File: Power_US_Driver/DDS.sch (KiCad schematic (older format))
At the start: 3 parts, among them U3 AD9833_MOD

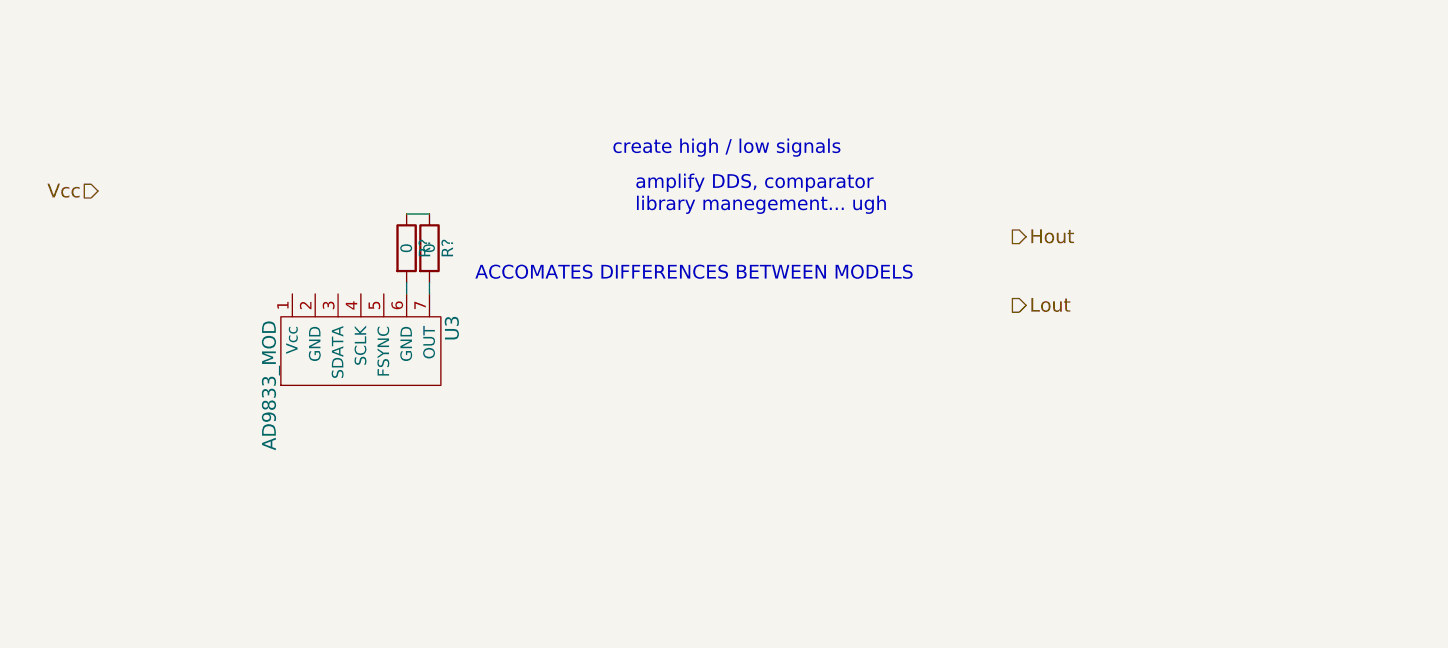
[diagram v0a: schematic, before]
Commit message: CURRENT SENSE REROUT, HIGHSIDE DRIVER GROUNDING
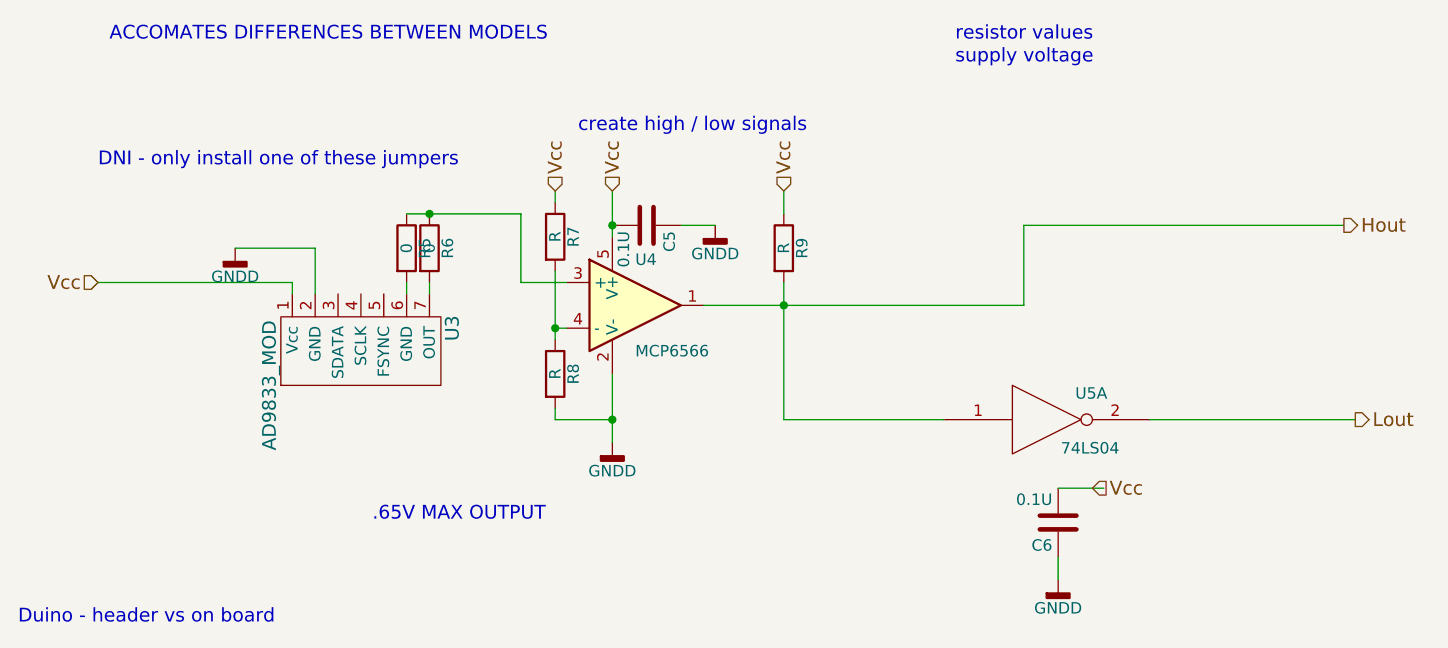
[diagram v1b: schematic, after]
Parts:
- added C5, C6: 0.1U, symbol C
- added R7, R8, R9: R, symbol R
- added U4: MCP6566, symbol MCP6566
- added U5: 74LS04, symbol 74LS04
- gave numbers to parts that had none: 2
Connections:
- net labels added: GNDD
- wire segments 3 -> 26
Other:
- note added: ".65V MAX OUTPUT"
- note added: "DNI - only install one of these jumpers"
- note added: "Duino - header vs on board"
- note added: "resistor values"
- note added: "supply voltage"
- note removed: "amplify DDS, comparator\nlibrary manegement... ugh"
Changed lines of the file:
@@
 LIBS:LIA-cache
 LIBS:power_US
+LIBS:JasMoH_Parts
 LIBS:Power_US_Driver-cache
 EELAYER 25 0
@@
 	0    -1   1    0
 $EndComp
-Text Notes 5450 3050 0    60   ~ 0
+Text Notes 5300 2950 0    60   ~ 0
 create high / low signals
-Text HLabel 3200 3200 0    60   Input ~ 0
-Vcc
-Text HLabel 7200 3400 2    60   Output ~ 0
+Text HLabel 3200 3600 0    60   Input ~ 0
+Vcc
+Text HLabel 8650 3350 2    60   Output ~ 0
 Hout
-Text HLabel 7200 3700 2    60   Output ~ 0
+Text HLabel 8700 4200 2    60   Output ~ 0
 Lout
-Text Notes 5550 3300 0    60   ~ 0
-amplify DDS, comparator\nlibrary manegement... ugh
-$Comp
-L R R?
+$Comp
+L R R5
 U 1 1 5AB00777
 P 4550 3450
-F 0 "R?" V 4630 3450 50  0000 C CNN
+F 0 "R5" V 4630 3450 50  0000 C CNN
 F 1 "0" V 4550 3450 50  0000 C CNN
 F 2 "" V 4480 3450 50  0001 C CNN
@@
 $EndComp
 $Comp
-L R R?
+L R R6
 U 1 1 5AB0079E
 P 4650 3450
-F 0 "R?" V 4730 3450 50  0000 C CNN
+F 0 "R6" V 4730 3450 50  0000 C CNN
 F 1 "0" V 4650 3450 50  0000 C CNN
 F 2 "" V 4580 3450 50  0001 C CNN
@@
 	1    0    0    -1
 $EndComp
-Wire Wire Line
-	4650 3300 4550 3300
+Text Notes 3250 2550 0    60   ~ 0
+ACCOMATES DIFFERENCES BETWEEN MODELS
+$Comp
+L GNDD #PWR5
+U 1 1 5AB1401C
+P 5450 4300
+F 0 "#PWR5" H 5450 4050 50  0001 C CNN
+F 1 "GNDD" H 5450 4175 50  0000 C CNN
+F 2 "" H 5450 4300 50  0001 C CNN
+F 3 "" H 5450 4300 50  0001 C CNN
+	1    5450 4300
+	1    0    0    -1
+$EndComp
+$Comp
+L GNDD #PWR4
+U 1 1 5AB14043
+P 3800 3450
+F 0 "#PWR4" H 3800 3200 50  0001 C CNN
+F 1 "GNDD" H 3800 3325 50  0000 C CNN
+F 2 "" H 3800 3450 50  0001 C CNN
+F 3 "" H 3800 3450 50  0001 C CNN
+	1    3800 3450
+	1    0    0    -1
+$EndComp
+Text Notes 2850 5100 0    60   ~ 0
+Duino - header vs on board
+Text HLabel 5450 3200 1    60   Input ~ 0
+Vcc
+Text HLabel 6200 3200 1    60   Input ~ 0
+Vcc
+Text HLabel 5200 3200 1    60   Input ~ 0
+Vcc
+$Comp
+L R R7
+U 1 1 5AB144B5
+P 5200 3400
+F 0 "R7" V 5280 3400 50  0000 C CNN
+F 1 "R" V 5200 3400 50  0000 C CNN
+F 2 "" V 5130 3400 50  0001 C CNN
+F 3 "" H 5200 3400 50  0001 C CNN
+	1    5200 3400
+	1    0    0    -1
+$EndComp
+$Comp
+L R R8
+U 1 1 5AB144D7
+P 5200 4000
+F 0 "R8" V 5280 4000 50  0000 C CNN
+F 1 "R" V 5200 4000 50  0000 C CNN
+F 2 "" V 5130 4000 50  0001 C CNN
+F 3 "" H 5200 4000 50  0001 C CNN
+	1    5200 4000
+	1    0    0    -1
+$EndComp
+$Comp
+L R R9
+U 1 1 5AB14525
+P 6200 3450
+F 0 "R9" V 6280 3450 50  0000 C CNN
+F 1 "R" V 6200 3450 50  0000 C CNN
+F 2 "" V 6130 3450 50  0001 C CNN
+F 3 "" H 6200 3450 50  0001 C CNN
+	1    6200 3450
+	1    0    0    -1
+$EndComp
+$Comp
+L C C5
+U 1 1 5AB14711
+P 5600 3350
+F 0 "C5" H 5625 3450 50  0000 L CNN
+F 1 "0.1U" H 5625 3250 50  0000 L CNN
+F 2 "" H 5638 3200 50  0001 C CNN
+F 3 "" H 5600 3350 50  0001 C CNN
+	1    5600 3350
+	0    1    1    0
+$EndComp
+$Comp
+L GNDD #PWR6
+U 1 1 5AB14762
+P 5900 3350
+F 0 "#PWR6" H 5900 3100 50  0001 C CNN
+F 1 "GNDD" H 5900 3225 50  0000 C CNN
+F 2 "" H 5900 3350 50  0001 C CNN
+F 3 "" H 5900 3350 50  0001 C CNN
+	1    5900 3350
+	1    0    0    -1
+$EndComp
+Text Notes 3200 3100 0    60   ~ 0
+DNI - only install one of these jumpers
+$Comp
+L 74LS04 U5
+U 1 1 5AB14D68
+P 7350 4200
+F 0 "U5" H 7545 4315 50  0000 C CNN
+F 1 "74LS04" H 7540 4075 50  0000 C CNN
+F 2 "" H 7350 4200 50  0001 C CNN
+F 3 "" H 7350 4200 50  0001 C CNN
+	1    7350 4200
+	1    0    0    -1
+$EndComp
+$Comp
+L MCP6566 U4
+U 1 1 5AB13E1C
+P 5550 3700
+F 0 "U4" H 5550 3900 50  0000 L CNN
+F 1 "MCP6566" H 5550 3500 50  0000 L CNN
+F 2 "" H 5550 3300 50  0001 C CNN
+F 3 "" H 5550 3700 50  0001 C CNN
+	1    5550 3700
+	1    0    0    -1
+$EndComp
+Wire Wire Line
+	6200 4200 6900 4200
+Connection ~ 6200 3700
+Wire Wire Line
+	7250 3350 7250 3700
+Wire Wire Line
+	8650 3350 7250 3350
+Wire Wire Line
+	7800 4200 8700 4200
+Wire Wire Line
+	5200 3250 5200 3200
+Wire Wire Line
+	6200 3600 6200 4200
+Wire Wire Line
+	7250 3700 5850 3700
+Wire Wire Line
+	6200 3200 6200 3300
+Connection ~ 5450 3350
+Wire Wire Line
+	5900 3350 5750 3350
+Connection ~ 5450 4200
+Wire Wire Line
+	5200 4200 5450 4200
+Wire Wire Line
+	5200 4150 5200 4200
+Connection ~ 5200 3800
+Wire Wire Line
+	5250 3800 5200 3800
+Wire Wire Line
+	5200 3550 5200 3850
+Connection ~ 4650 3300
+Wire Wire Line
+	5050 3600 5250 3600
+Wire Wire Line
+	5050 3300 5050 3600
+Wire Wire Line
+	5450 3200 5450 3400
+Wire Wire Line
+	4050 3600 3200 3600
+Wire Wire Line
+	4050 3650 4050 3600
+Wire Wire Line
+	4150 3450 4150 3650
+Wire Wire Line
+	3800 3450 4150 3450
+Wire Wire Line
+	5450 4300 5450 4000
+Wire Wire Line
+	4550 3600 4550 3650
 Wire Wire Line
 	4650 3600 4650 3650
 Wire Wire Line
-	4550 3600 4550 3650
-Text Notes 4850 3600 0    60   ~ 0
-ACCOMATES DIFFERENCES BETWEEN MODELS
+	4550 3300 5050 3300
+Text Notes 6950 2550 0    60   ~ 0
+resistor values
+Text Notes 6950 2650 0    60   ~ 0
+supply voltage
+Text HLabel 7550 4500 2    60   Input ~ 0
+Vcc
+$Comp
+L C C6
+U 1 1 5AB155A5
+P 7400 4650
+F 0 "C6" H 7425 4750 50  0000 L CNN
+F 1 "0.1U" H 7425 4550 50  0000 L CNN
+F 2 "" H 7438 4500 50  0001 C CNN
+F 3 "" H 7400 4650 50  0001 C CNN
+	1    7400 4650
+	-1   0    0    1
+$EndComp
+$Comp
+L GNDD #PWR7
+U 1 1 5AB15619
+P 7400 4900
+F 0 "#PWR7" H 7400 4650 50  0001 C CNN
+F 1 "GNDD" H 7400 4775 50  0000 C CNN
+F 2 "" H 7400 4900 50  0001 C CNN
+F 3 "" H 7400 4900 50  0001 C CNN
+	1    7400 4900
+	1    0    0    -1
+$EndComp
+Wire Wire Line
+	7600 4500 7400 4500
+Wire Wire Line
+	7400 4800 7400 4900
+Text Notes 4400 4650 0    60   ~ 0
+.65V MAX OUTPUT
 $EndSCHEMATC
